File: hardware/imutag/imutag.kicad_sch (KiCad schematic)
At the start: 26 parts, among them J201 CONN_02X04, J301 Conn_01x01, J302 Conn_01x01, J303 Conn_01x01, J304 Conn_01x01, J401 CONN_01X02, Q501 Q_NPN_BEC, U1 at25ex321D-UUN, U2 AK09940A, U3 LPS22DF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

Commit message: checkpoint
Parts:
- removed Q501: Q_NPN_BEC, Package_TO_SOT_SMD:SOT-883, symbol Device:Q_NPN_BEC
- J401: footprint AccelTag:MS621 -> AccelTag:batterypads
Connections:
- net VBAT: now also D401.2 (A); no longer C7.1, D401.1 (K), U4.3 (EN), U4.4 (IN)
- net VIN: now also C7.1, D401.1 (K), U4.3 (EN), U4.4 (IN); no longer D401.2 (A)
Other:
- note added: "Cap shared with adjacent devices"
- note added: "Switch Mag and IMU ??"
- moved on the sheet: D401

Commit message: checkpoint
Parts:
- added Q501: Q_NPN_BEC, Package_TO_SOT_SMD:SOT-883, symbol Device:Q_NPN_BEC
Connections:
- net AK_CS: now also U302.7 (PA1); no longer U302.15 (PB1)
- net GND: now also Q501.2 (E)
- net RST: now also Q501.1 (B)
- net at C502.1, U302.4 (~{NRST}): now also Q501.3 (C)
- net ACCEL_CS renamed LSM_CS
- net LSM_CS: now also U302.15 (PB1); no longer U302.7 (PA1)
- net AK_CK renamed AK_USART2_CK
- net AK_USART2_CK: now also U302.10 (PA4); no longer U302.11 (PA5)
- net AK_MISO renamed AK_USART2_RX
- net AK_USART2_RX: now also U302.9 (PA3); no longer U302.12 (PA6)
- net AK_MOSI renamed AK_USART2_TX
- net AK_USART2_TX: now also U302.8 (PA2); no longer U302.13 (PA7)
- net USART2_CK renamed LSM_CK
- net LSM_CK: now also U302.11 (PA5); no longer U302.10 (PA4)
- net USART2_RX renamed LSM_MISO
- net LSM_MISO: now also U302.12 (PA6); no longer U302.9 (PA3)
- net USART2_TX renamed LSM_MOSI
- net LSM_MOSI: now also U302.13 (PA7); no longer U302.8 (PA2)
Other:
- moved on the sheet: C2

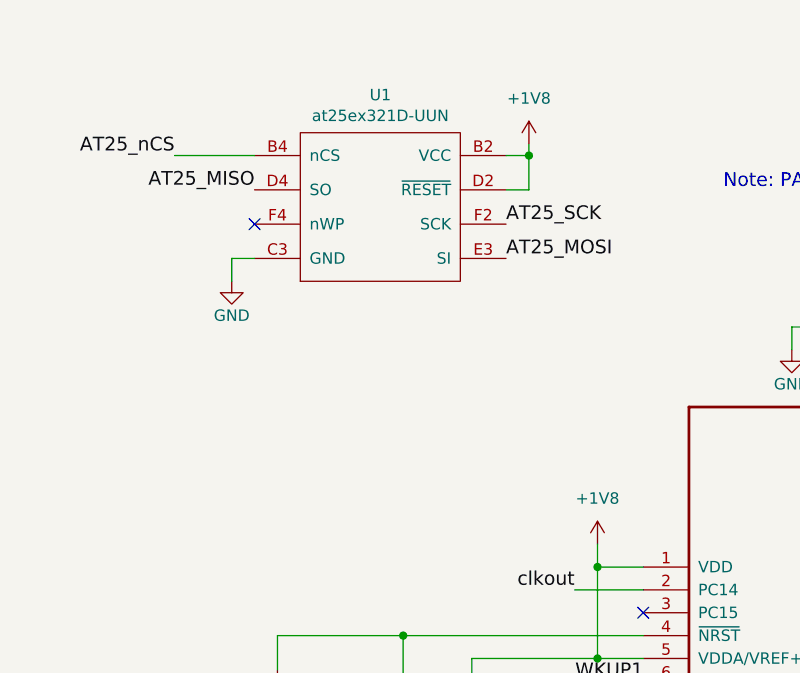
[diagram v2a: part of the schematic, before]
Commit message: update flash for imu tag
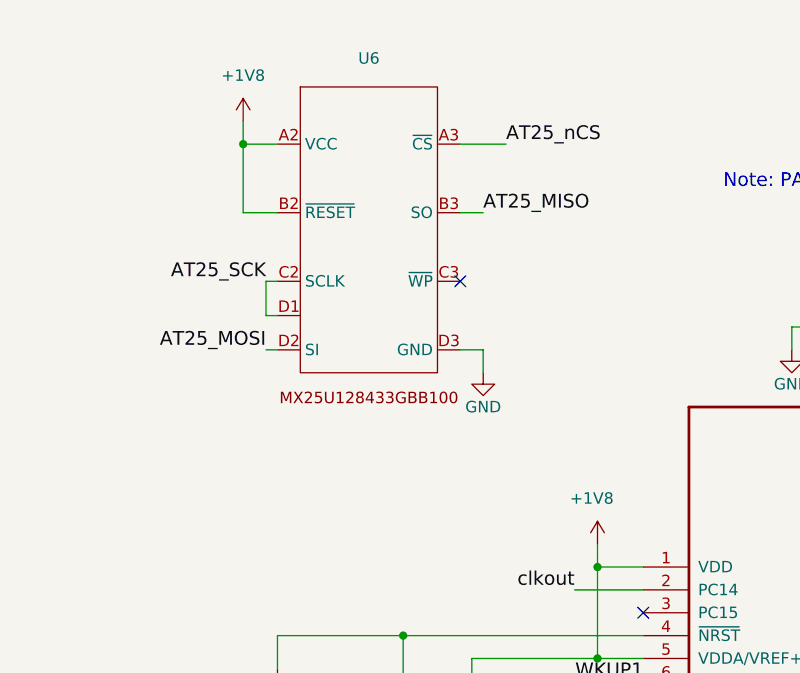
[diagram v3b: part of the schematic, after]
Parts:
- removed U1: at25ex321D-UUN, AccelTag:adesto_wlcsp12, symbol BitTagNG:at25ex321D-UUN-AccelTag
- added U6: ~, AccelTag:IC_MX25U12843GBBI00, symbol mx25:MX25U12843GBBI00
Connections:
- net +1V8: now also U6.A2 (VCC), U6.B2 (~{RESET})
- net AT25_MISO: now also U6.B3 (SO)
- net AT25_MOSI: now also U6.D2 (SI)
- net AT25_SCK: now also U6.C2 (SCLK), U6.D1
- net AT25_nCS: now also U6.A3 (~{CS})
- net GND: now also U6.D3 (GND)

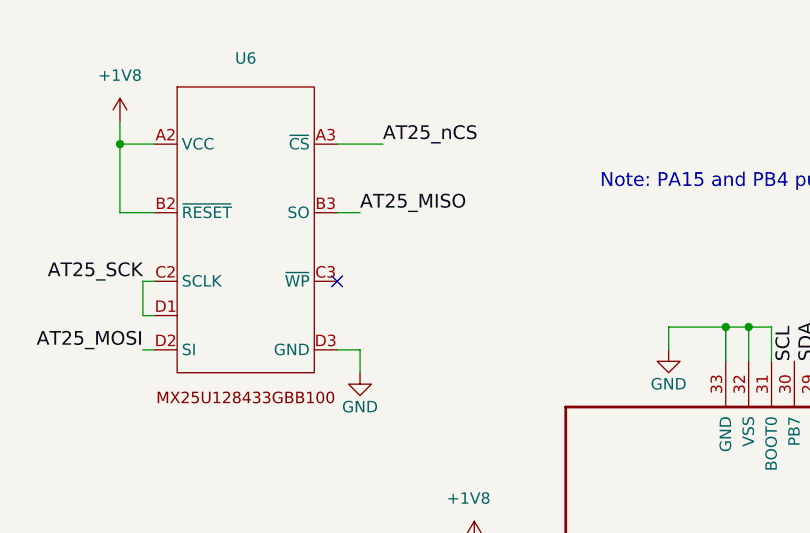
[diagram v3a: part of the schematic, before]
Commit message: added nucleoshield template
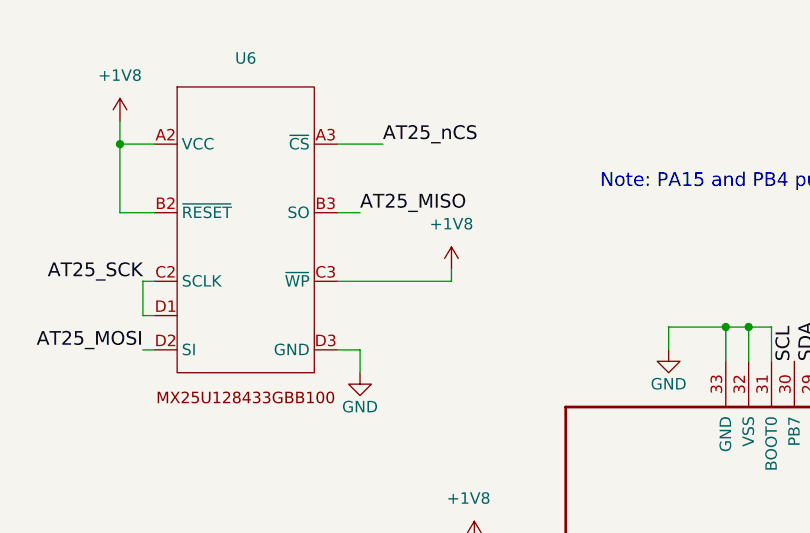
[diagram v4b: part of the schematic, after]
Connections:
- net +1V8: now also U6.C3 (~{WP})
- no-connect marks 9 -> 8
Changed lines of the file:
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@@
 	)
 	(no_connect
-		(at 67.31 44.45)
-	)
-	(no_connect
 		(at 242.57 135.89)
 	)
@@
 	(wire
 		(pts
+			(xy 80.01 44.45) (xy 80.01 43.18)
+		)
+		(stroke
+			(width 0)
+			(type default)
+		)
+	)
+	(wire
+		(pts
 			(xy 153.67 78.74) (xy 153.67 74.93)
 		)
@@
 	(wire
 		(pts
+			(xy 67.31 44.45) (xy 80.01 44.45)
+		)
+		(stroke
+			(width 0)
+			(type default)
+		)
+	)
+	(wire
+		(pts
 			(xy 172.72 29.21) (xy 191.77 29.21)
 		)
@@
 					(unit 1)
 				)
+			)
+		)
+	)
+	(symbol
+		(lib_id "power:+1V8")
+		(at 80.01 43.18 0)
+		(unit 1)
+		(exclude_from_sim no)
+		(in_bom yes)
+		(on_board yes)
+		(dnp no)
+		(fields_autoplaced yes)
+		(property "Reference" "#PWR10"
+			(at 80.01 46.99 0)
+			(effects
+				(font
+					(size 1.27 1.27)
+				)
+				(hide yes)
+			)
+		)
+		(property "Value" "+1V8"
+			(at 80.01 38.1 0)
+			(effects
+				(font
+					(size 1.27 1.27)
+				)
+			)
+		)
+		(property "Footprint" ""
+			(at 80.01 43.18 0)
+			(effects
+				(font
+					(size 1.27 1.27)
+				)
+				(hide yes)
+			)
+		)
+		(property "Datasheet" ""
+			(at 80.01 43.18 0)
+			(effects
+				(font
+					(size 1.27 1.27)
+				)
+				(hide yes)
+			)
+		)
+		(property "Description" "Power symbol creates a global label with name \"+1V8\""
+			(at 80.01 43.18 0)
+			(effects
+				(font
+					(size 1.27 1.27)
+				)
+				(hide yes)
+			)
+		)
+		(pin "1"
+		)
+		(instances
+			(project "imutag"
+				(path "/e44ca67a-43be-444b-8652-f54825a2eb6f"
+					(reference "#PWR10")
+					(unit 1)
+				)
